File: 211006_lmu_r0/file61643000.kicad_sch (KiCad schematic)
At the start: 6 parts, among them J9 Conn_01x02, K1 G5V-2 DC-3, Q38 BC817

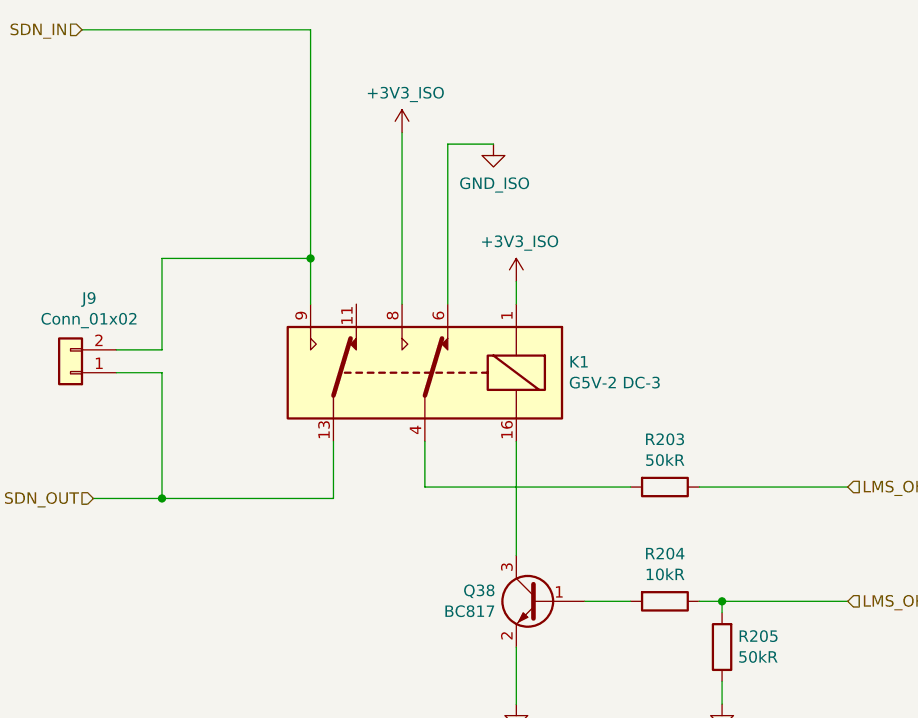
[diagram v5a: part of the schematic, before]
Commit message: silkscreen changes, shifting bun leds
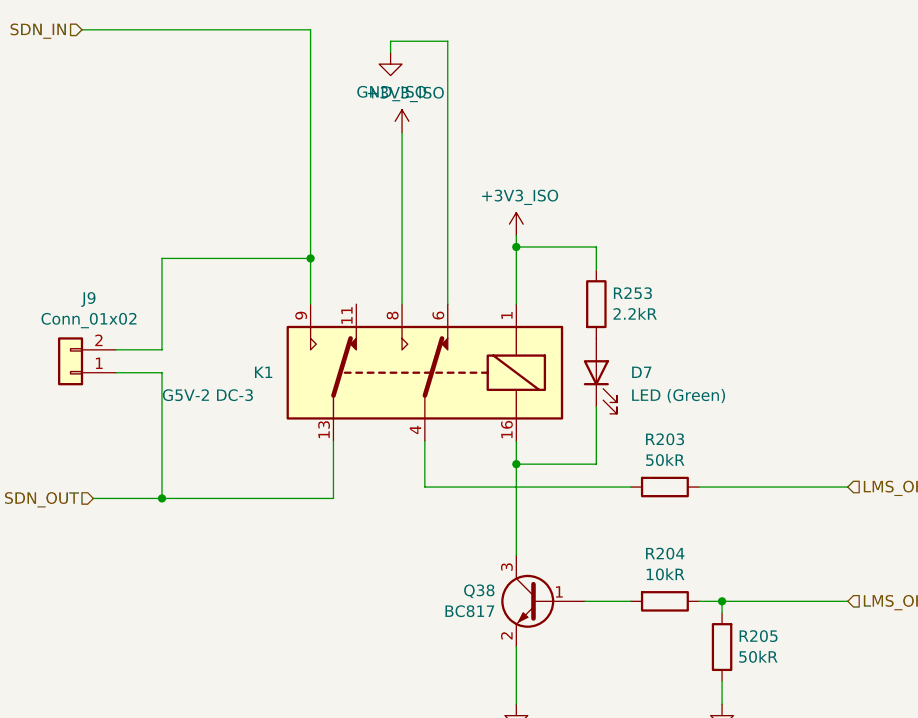
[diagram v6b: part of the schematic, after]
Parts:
- added D7: LED (Green), LED_SMD:LED_0805_2012Metric_Pad1.15x1.40mm_HandSolder, symbol Device:LED
- added R253: 2.2kR, Resistor_SMD:R_0603_1608Metric_Pad0.98x0.95mm_HandSolder, symbol Device:R
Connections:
- net +3V3_ISO: now also R253.1
- net at K1.16, Q38.3 (C): now also D7.1 (K)
- new net: D7.2 (A), R253.2
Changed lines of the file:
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@@
 (kicad_sch (version 20211123) (generator eeschema)
   (paper "A4")
+  (junction (at 151.13 91.44) (diameter 0) (color 0 0 0 0)
+  )
+  (junction (at 151.13 67.31) (diameter 0) (color 0 0 0 0)
+  )
   (junction (at 111.76 95.25) (diameter 0) (color 0 0 0 0)
   )
@@
   (junction (at 173.99 106.68) (diameter 0) (color 0 0 0 0)
   )
+  (wire (pts (xy 151.13 91.44) (xy 151.13 101.6))
+    (stroke (width 0) (type default) (color 0 0 0 0))
+  )
   (wire (pts (xy 163.83 93.98) (xy 140.97 93.98))
     (stroke (width 0) (type default) (color 0 0 0 0))
@@
     (stroke (width 0) (type default) (color 0 0 0 0))
   )
-  (wire (pts (xy 151.13 88.9) (xy 151.13 101.6))
+  (wire (pts (xy 151.13 88.9) (xy 151.13 91.44))
+    (stroke (width 0) (type default) (color 0 0 0 0))
+  )
+  (wire (pts (xy 160.02 67.31) (xy 151.13 67.31))
     (stroke (width 0) (type default) (color 0 0 0 0))
   )
@@
     (stroke (width 0) (type default) (color 0 0 0 0))
   )
+  (wire (pts (xy 137.16 44.45) (xy 143.51 44.45))
+    (stroke (width 0) (type default) (color 0 0 0 0))
+  )
+  (wire (pts (xy 151.13 67.31) (xy 151.13 73.66))
+    (stroke (width 0) (type default) (color 0 0 0 0))
+  )
+  (wire (pts (xy 137.16 44.45) (xy 137.16 45.72))
+    (stroke (width 0) (type default) (color 0 0 0 0))
+  )
   (wire (pts (xy 102.87 43.18) (xy 128.27 43.18))
     (stroke (width 0) (type default) (color 0 0 0 0))
   )
-  (wire (pts (xy 143.51 55.88) (xy 148.59 55.88))
-    (stroke (width 0) (type default) (color 0 0 0 0))
-  )
   (wire (pts (xy 187.96 93.98) (xy 171.45 93.98))
     (stroke (width 0) (type default) (color 0 0 0 0))
@@
     (stroke (width 0) (type default) (color 0 0 0 0))
   )
+  (wire (pts (xy 160.02 85.09) (xy 160.02 91.44))
+    (stroke (width 0) (type default) (color 0 0 0 0))
+  )
   (wire (pts (xy 151.13 111.76) (xy 151.13 118.11))
     (stroke (width 0) (type default) (color 0 0 0 0))
@@
     (stroke (width 0) (type default) (color 0 0 0 0))
   )
+  (wire (pts (xy 160.02 67.31) (xy 160.02 69.85))
+    (stroke (width 0) (type default) (color 0 0 0 0))
+  )
   (wire (pts (xy 171.45 106.68) (xy 173.99 106.68))
     (stroke (width 0) (type default) (color 0 0 0 0))
@@
     (stroke (width 0) (type default) (color 0 0 0 0))
   )
-  (wire (pts (xy 151.13 71.12) (xy 151.13 73.66))
+  (wire (pts (xy 151.13 66.04) (xy 151.13 67.31))
     (stroke (width 0) (type default) (color 0 0 0 0))
   )
@@
     (stroke (width 0) (type default) (color 0 0 0 0))
   )
-  (wire (pts (xy 143.51 55.88) (xy 143.51 73.66))
+  (wire (pts (xy 143.51 44.45) (xy 143.51 73.66))
     (stroke (width 0) (type default) (color 0 0 0 0))
   )
   (wire (pts (xy 111.76 81.28) (xy 111.76 95.25))
+    (stroke (width 0) (type default) (color 0 0 0 0))
+  )
+  (wire (pts (xy 151.13 91.44) (xy 160.02 91.44))
     (stroke (width 0) (type default) (color 0 0 0 0))
   )
@@
   (symbol (lib_id "Relay:G5V-2") (at 140.97 81.28 0) (mirror y) (unit 1)
     (in_bom yes) (on_board yes)
-    (property "Reference" "K1" (id 0) (at 156.972 80.1116 0)
-      (effects (font (size 1.27 1.27)) (justify right))
-    )
-    (property "Value" "G5V-2 DC-3" (id 1) (at 156.972 82.423 0)
+    (property "Reference" "K1" (id 0) (at 121.92 81.28 0)
+      (effects (font (size 1.27 1.27)) (justify right))
+    )
+    (property "Value" "G5V-2 DC-3" (id 1) (at 111.76 83.82 0)
       (effects (font (size 1.27 1.27)) (justify right))
     )
@@
     (pin "2")
   )
-  (symbol (lib_name "GND_ISO_2") (lib_id "gnd_iso:GND_ISO") (at 148.59 55.88 0) (unit 1)
-    (in_bom yes) (on_board yes)
-    (property "Reference" "#PWR067" (id 0) (at 148.59 62.23 0)
-      (effects (font (size 1.27 1.27)) hide)
-    )
-    (property "Value" "GND_ISO" (id 1) (at 148.717 60.2742 0))
-    (property "Footprint" "" (id 2) (at 148.59 55.88 0)
-      (effects (font (size 1.27 1.27)) hide)
-    )
-    (property "Datasheet" "" (id 3) (at 148.59 55.88 0)
-      (effects (font (size 1.27 1.27)) hide)
-    )
-    (pin "1")
-  )
-  (symbol (lib_name "+3V3_ISO_1") (lib_id "+3v3_iso:+3V3_ISO") (at 151.13 71.12 0) (unit 1)
-    (in_bom yes) (on_board yes)
-    (property "Reference" "#PWR068" (id 0) (at 151.13 74.93 0)
-      (effects (font (size 1.27 1.27)) hide)
-    )
-    (property "Value" "+3V3_ISO" (id 1) (at 151.511 66.7258 0))
-    (property "Footprint" "" (id 2) (at 151.13 71.12 0)
-      (effects (font (size 1.27 1.27)) hide)
-    )
-    (property "Datasheet" "" (id 3) (at 151.13 71.12 0)
+  (symbol (lib_name "GND_ISO_2") (lib_id "gnd_iso:GND_ISO") (at 137.16 45.72 0) (unit 1)
+    (in_bom yes) (on_board yes)
+    (property "Reference" "#PWR067" (id 0) (at 137.16 52.07 0)
+      (effects (font (size 1.27 1.27)) hide)
+    )
+    (property "Value" "GND_ISO" (id 1) (at 137.287 50.1142 0))
+    (property "Footprint" "" (id 2) (at 137.16 45.72 0)
+      (effects (font (size 1.27 1.27)) hide)
+    )
+    (property "Datasheet" "" (id 3) (at 137.16 45.72 0)
+      (effects (font (size 1.27 1.27)) hide)
+    )
+    (pin "1")
+  )
+  (symbol (lib_name "+3V3_ISO_1") (lib_id "+3v3_iso:+3V3_ISO") (at 151.13 66.04 0) (unit 1)
+    (in_bom yes) (on_board yes)
+    (property "Reference" "#PWR068" (id 0) (at 151.13 69.85 0)
+      (effects (font (size 1.27 1.27)) hide)
+    )
+    (property "Value" "+3V3_ISO" (id 1) (at 151.511 61.6458 0))
+    (property "Footprint" "" (id 2) (at 151.13 66.04 0)
+      (effects (font (size 1.27 1.27)) hide)
+    )
+    (property "Datasheet" "" (id 3) (at 151.13 66.04 0)
       (effects (font (size 1.27 1.27)) hide)
     )
@@
       (effects (font (size 1.27 1.27)) hide)
     )
+    (pin "1")
+    (pin "2")
+  )
+  (symbol (lib_id "Device:LED") (at 160.02 81.28 90) (unit 1)
+    (in_bom yes) (on_board yes)
+    (property "Reference" "D7" (id 0) (at 163.83 81.28 90)
+      (effects (font (size 1.27 1.27)) (justify right))
+    )
+    (property "Value" "LED (Green)" (id 1) (at 163.83 83.82 90)
+      (effects (font (size 1.27 1.27)) (justify right))
+    )
+    (property "Footprint" "LED_SMD:LED_0805_2012Metric_Pad1.15x1.40mm_HandSolder" (id 2) (at 160.02 81.28 0)
+      (effects (font (size 1.27 1.27)) hide)
+    )
+    (property "Datasheet" "~" (id 3) (at 160.02 81.28 0)
+      (effects (font (size 1.27 1.27)) hide)
+    )
+    (property "Manufacturer" "AMS OSRAM" (id 4) (at 160.02 81.28 0)
+      (effects (font (size 1.27 1.27)) hide)
+    )
+    (property "Mouser Part Number" "720-LSR976-NR-1" (id 5) (at 160.02 81.28 0)
+      (effects (font (size 1.27 1.27)) hide)
+    )
+    (property "Mouser URL" "https://au.mouser.com/ProductDetail/ams-OSRAM/LS-R976-NR-1-0-20-R18?qs=sGAEpiMZZMt82OzCyDsLFGbrp1fQkD8H8bij58Oys9s%3D" (id 6) (at 160.02 81.28 0)
+      (effects (font (size 1.27 1.27)) hide)
+    )
+    (property "Part Number" "LS R976-NR-1-0-20-R18" (id 7) (at 160.02 81.28 0)
+      (effects (font (size 1.27 1.27)) hide)
+    )
+    (pin "1")
+    (pin "2")
+  )
+  (symbol (lib_id "Device:R") (at 160.02 73.66 0) (unit 1)
+    (in_bom yes) (on_board yes)
+    (property "Reference" "R253" (id 0) (at 161.798 72.4916 0)
+      (effects (font (size 1.27 1.27)) (justify left))
+    )
+    (property "Value" "2.2kR" (id 1) (at 161.798 74.803 0)
+      (effects (font (size 1.27 1.27)) (justify left))
+    )
+    (property "Footprint" "Resistor_SMD:R_0603_1608Metric_Pad0.98x0.95mm_HandSolder" (id 2) (at 158.242 73.66 90)
+      (effects (font (size 1.27 1.27)) hide)
+    )
+    (property "Datasheet" "~" (id 3) (at 160.02 73.66 0)
+      (effects (font (size 1.27 1.27)) hide)
+    )
+    (property "Part Number" "-" (id 4) (at 160.02 73.66 0)
+      (effects (font (size 1.27 1.27)) hide)
+    )
+    (property "Manufacturer" "-" (id 5) (at 160.02 73.66 0)
+      (effects (font (size 1.27 1.27)) hide)
+    )

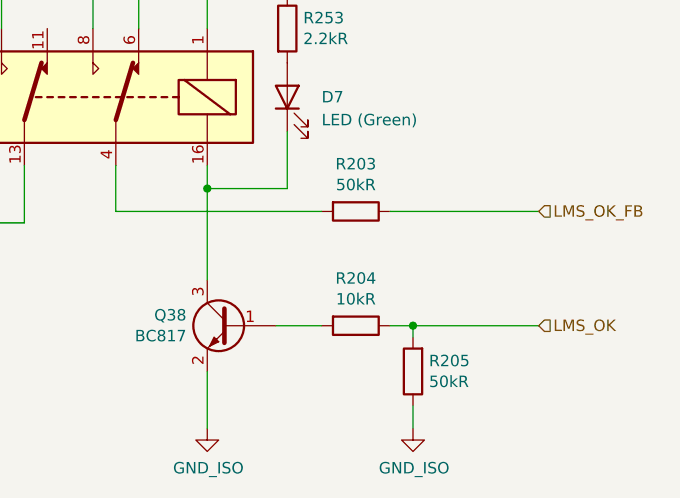
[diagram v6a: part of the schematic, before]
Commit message: going to bulk edit fields
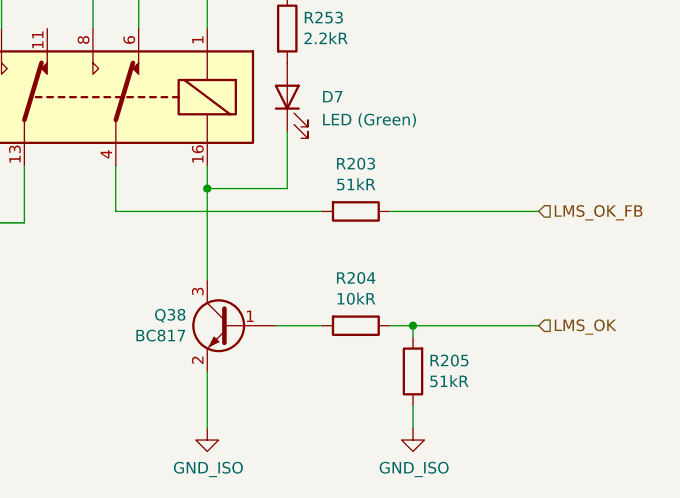
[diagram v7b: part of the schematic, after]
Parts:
- R203, R205: value 50kR -> 51kR
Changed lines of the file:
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@@
       (effects (font (size 1.27 1.27)) (justify right))
     )
-    (property "Value" "50kR" (id 1) (at 175.768 112.903 0)
+    (property "Value" "51kR" (id 1) (at 175.768 112.903 0)
       (effects (font (size 1.27 1.27)) (justify right))
     )
@@
     (in_bom yes) (on_board yes)
     (property "Reference" "R203" (id 0) (at 167.64 88.7222 90))
-    (property "Value" "50kR" (id 1) (at 167.64 91.0336 90))
+    (property "Value" "51kR" (id 1) (at 167.64 91.0336 90))
     (property "Footprint" "Resistor_SMD:R_0603_1608Metric_Pad0.98x0.95mm_HandSolder" (id 2) (at 167.64 92.202 90)
       (effects (font (size 1.27 1.27)) hide)
